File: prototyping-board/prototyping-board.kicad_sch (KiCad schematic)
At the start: 44 parts, among them J1 Conn_01x02, J10 Conn_01x02, J11 Conn_01x03, J12 Conn_01x03, J13 Conn_01x03, J14 Conn_01x03, J15 Conn_01x03, J16 Conn_01x03, J17 Conn_01x03, J18 Conn_01x03, J19 Conn_01x03, J2 Conn_01x02, J20 Conn_01x03, J21 Conn_01x03, J22 Conn_01x03, J23 Conn_01x06, J24 Conn_01x06, J25 Conn_01x04, J26 Conn_01x04, J27 Conn_01x05, J28 Conn_01x05, J29 Conn_01x05, J3 Conn_01x02, J30 Conn_01x04, J31 Conn_01x04, J32 Conn_01x04, J33 Conn_01x03, J34 Conn_01x03, J35 Conn_01x03, J36 Conn_01x02, J37 Conn_01x02, J38 Conn_01x02, J4 Conn_01x02, J5 Conn_01x02, J6 Conn_01x02, J7 Conn_01x02, J8 Conn_01x02, J9 Conn_01x02, U1 MEGA_PRO_EMBED_CH340G___ATMEG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

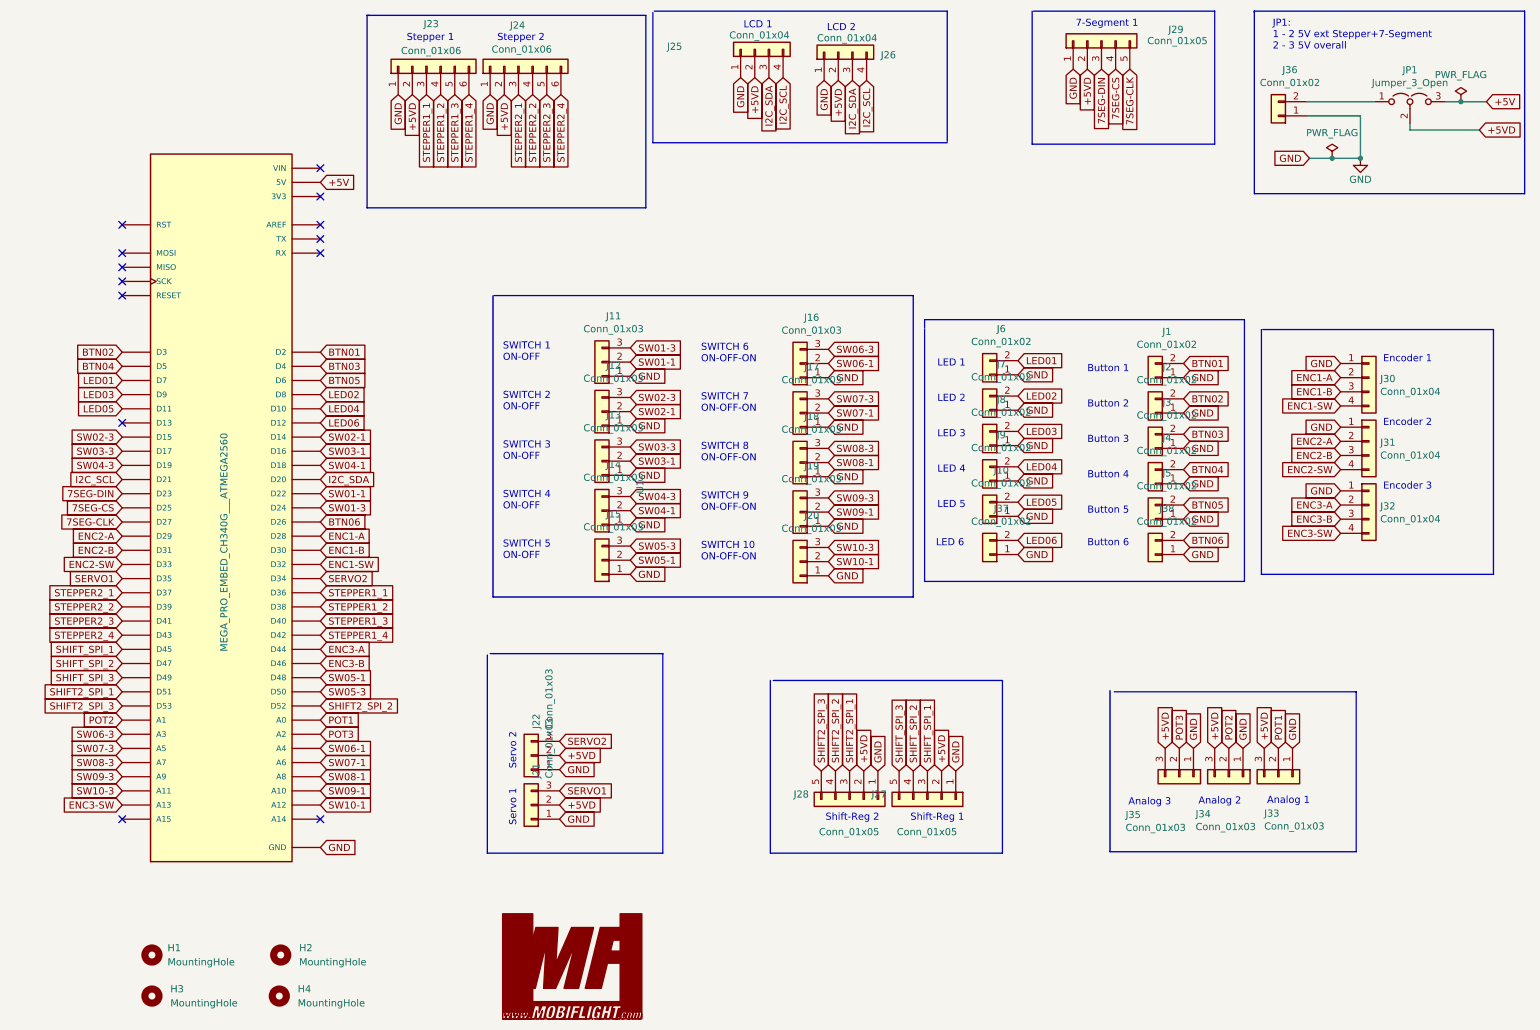
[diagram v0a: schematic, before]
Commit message: Prototype without power jumper
* add diode, add 4th Encoder, new position of PWR

* PWR connector in red, some optimazations

* ENC4 switch to Button 6

* update readme with shared pins

* LED6 to D13, ENC4 switch to D12

* update MegaMini symbol

* add a reset button, update readme accordingly

* add board config for board version 2.2

* fix wrong spelling
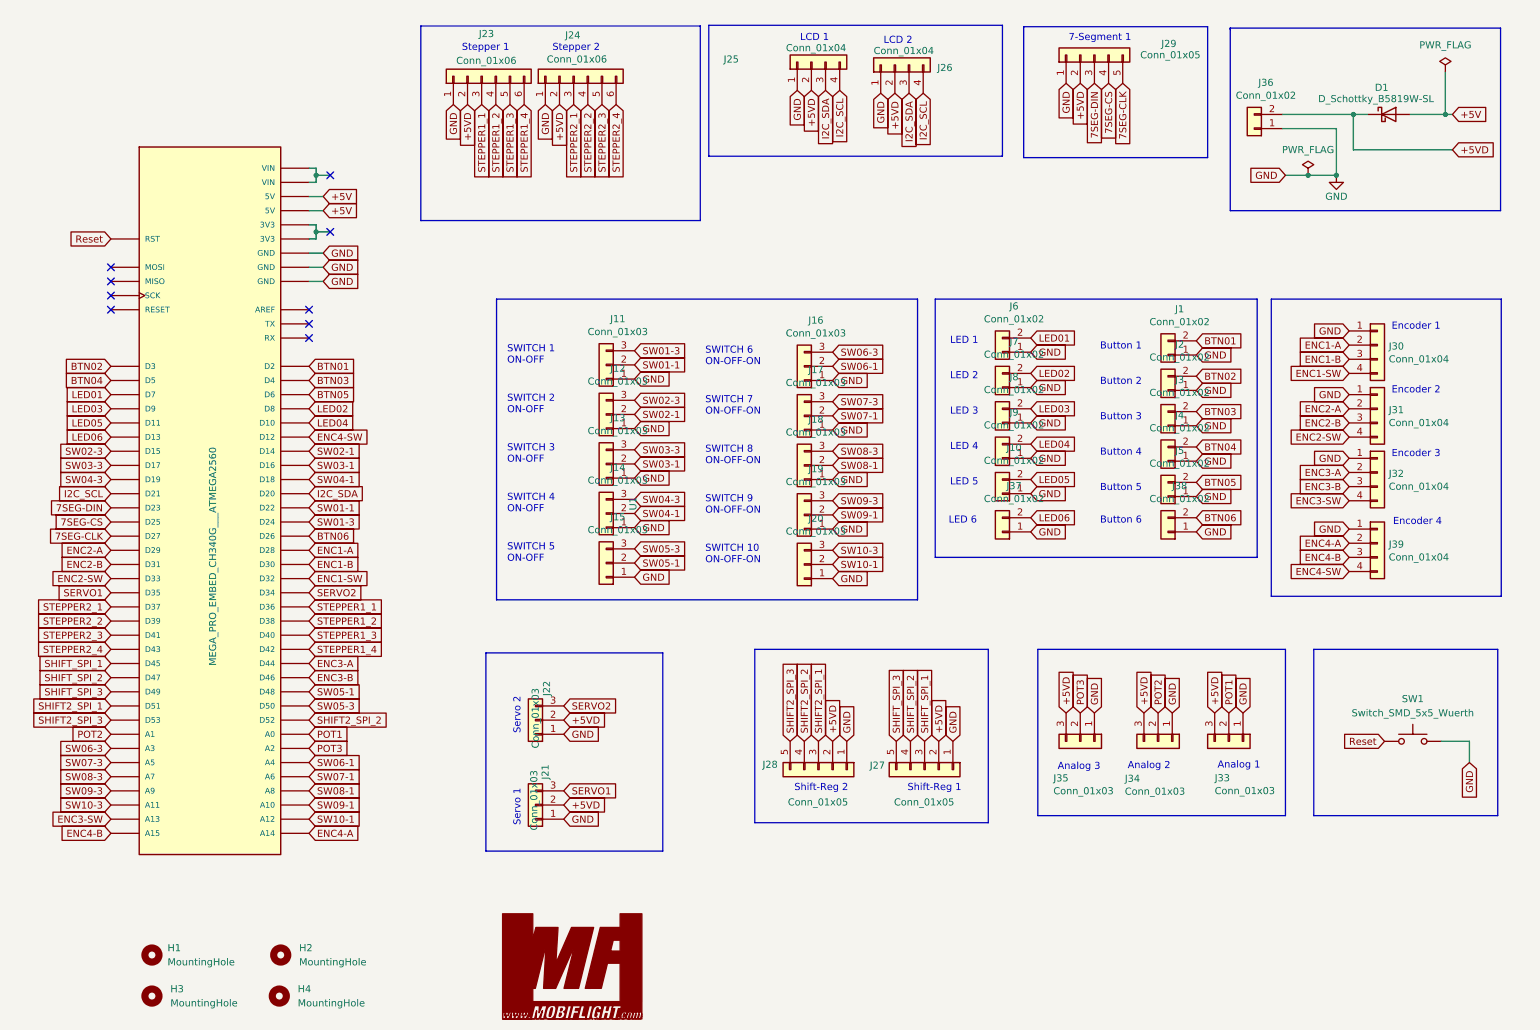
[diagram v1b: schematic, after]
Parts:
- removed JP1: Jumper_3_Open, Connector_PinHeader_2.54mm:PinHeader_1x03_P2.54mm_Vertical, symbol Jumper:Jumper_3_Open
- added D1: D_Schottky_B5819W-SL, Diode_SMD:D_SOD-123, symbol MobiFlight:D_Schottky_B5819W-SL
- added J39: Conn_01x04, Connector_JST:JST_XH_B4B-XH-A_1x04_P2.50mm_Vertical, symbol Connector_Generic:Conn_01x04
- added SW1: Switch_SMD_5x5_Wuerth, MobiFlight:SW_Push_1P1T_NO_Vertical_Wuerth_434133025816, symbol MobiFlight:Switch_SMD_5x5_Wuerth
- J36: LCSC C20079 -> C24192
- U1: symbol mobiflight-library:MEGA_PRO_EMBED_CH340G___ATMEGA2560 -> MobiFlight:MEGA_PRO_EMBED_CH340G___ATMEGA2560; now left out of the parts list
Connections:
- net +5V: now also D1.2 (A); no longer U1.5V_3 (5V)
- net +5VD: now also J36.2 (Pin_2), D1.1 (K)
- net GND: now also J39.1 (Pin_1), SW1.2
- net LED06: now also U1.D13; no longer U1.D12
- net ENC4-A: now reaches U1.A14
- net ENC4-A: now also J39.2 (Pin_2)
- net ENC4-B: now reaches U1.A15
- net ENC4-B: now also J39.3 (Pin_3)
- net Reset: now reaches U1.RST
- net Reset: now also SW1.1
- new net ENC4-SW: J39.4 (Pin_4), U1.D12
- no-connect marks 13 -> 9
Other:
- note added: "Encoder 4"
- note removed: "JP1: 1 - 2 5V ext Stepper+7-Segment 2 - 3 5V overall"
- moved on the sheet: J1, J10, J11, J12, J13, J14, J15, J16, J17, J18, J19, J2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
